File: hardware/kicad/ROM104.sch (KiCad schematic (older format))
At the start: 27 parts, among them J1 Screw_Terminal_01x12, J2 CAN, K1 DIPxx-1Cxx-51x, K2 DIPxx-1Cxx-51x, K3 DIPxx-1Cxx-51x, K4 DIPxx-1Cxx-51x, SW1 INSTANCE, SW2 BUS, U1 L293D, U2 L293D, U3 MCP2551-I-P, U4 TMR_2411, U5 Teensy_3.2

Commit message: Update PCB
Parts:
- removed K1, K2, K3, K4: DIPxx-1Cxx-51x, PDJR-connectors:PE014F05, symbol Relay:DIPxx-1Cxx-51x
- removed R1, R2, R3, R4: 470R, Resistor_THT:R_Axial_DIN0207_L6.3mm_D2.5mm_P7.62mm_Horizontal, symbol Device:R
- added K1, K2, K3, K4: SPDT_RELAY, PDJR-connectors:PE014F05, symbol pdjr:SPDT_RELAY
- added RN1: 470R, Resistor_THT:R_Array_SIP5, symbol Device:R_Network04
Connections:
- net CH0_LED: now also D1.2 (A), U5.2 (D0/RX1); no longer U5.3 (D1/TX1)
- net CH1_LED: now also D2.2 (A), U5.3 (D1/TX1); no longer U5.2 (D0/RX1)
- net CH2_LED: now also D3.2 (A)
- net CH3_LED: now also D4.2 (A)
- net GND: now also RN1.1 (common); no longer D1.1 (K), D2.1 (K), D3.1 (K), D4.1 (K)
- net at J1.1 (Pin_1): now also K1.14
- net at J1.10 (Pin_10): now also K4.14
- net at J1.11 (Pin_11): now also K4.7
- net at J1.12 (Pin_12): now also K4.1
- net at J1.2 (Pin_2): now also K1.7
- net at J1.3 (Pin_3): now also K1.1
- net at J1.4 (Pin_4): now also K2.14
- net at J1.5 (Pin_5): now also K2.7
- net at J1.6 (Pin_6): now also K2.1
- net at J1.7 (Pin_7): now also K3.14
- net at J1.8 (Pin_8): now also K3.7
- net at J1.9 (Pin_9): now also K3.1
- net at U2.11 (3Y): now also K1.6
- net at U2.14 (4Y): now also K1.2
- net at U2.3 (1Y): now also K2.6
- net at U2.6 (2Y): now also K2.2
- net at U1.11 (3Y): now also K3.6
- net at U1.14 (4Y): now also K3.2
- net at U1.3 (1Y): now also K4.6
- net at U1.6 (2Y): now also K4.2
- new net: D1.1 (K), RN1.5 (R4)
- new net: D2.1 (K), RN1.4 (R3)
- new net: D3.1 (K), RN1.3 (R2)
- new net: D4.1 (K), RN1.2 (R1)
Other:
- moved on the sheet: D1, D2, D3, D4
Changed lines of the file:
@@
 Wire Wire Line
 	10450 1150 10450 2150
+Text Label 9550 5350 0    50   ~ 0
+CH0_LED
 Text Label 9550 5250 0    50   ~ 0
-CH0_LED
-Text Label 9550 5350 0    50   ~ 0
 CH1_LED
 Text Label 9550 5150 0    50   ~ 0
@@
 CH3_LED
 $Comp
-L Device:R R1
-U 1 1 631C1A0C
+L Device:LED D1
+U 1 1 631C329D
 P 4400 800
-F 0 "R1" V 4450 1000 50  0000 R CNN
-F 1 "470R" V 4400 800 39  0000 C CNN
-F 2 "Resistor_THT:R_Axial_DIN0207_L6.3mm_D2.5mm_P7.62mm_Horizontal" V 4330 800 50  0001 C CNN
+F 0 "D1" H 4500 750 50  0000 C CNN
+F 1 "LED" H 4393 636 50  0001 C CNN
+F 2 "LED_THT:LED_D1.8mm_W3.3mm_H2.4mm" H 4400 800 50  0001 C CNN
 F 3 "~" H 4400 800 50  0001 C CNN
 	1    4400 800
-	0    -1   -1   0
-$EndComp
-$Comp
-L Device:LED D1
-U 1 1 631C329D
-P 4800 800
-F 0 "D1" H 4900 750 50  0000 C CNN
-F 1 "LED" H 4793 636 50  0001 C CNN
-F 2 "LED_THT:LED_D1.8mm_W3.3mm_H2.4mm" H 4800 800 50  0001 C CNN
-F 3 "~" H 4800 800 50  0001 C CNN
-	1    4800 800
-	-1   0    0    1
-$EndComp
-Wire Wire Line
-	4550 800  4650 800
+	-1   0    0    1
+$EndComp
 Wire Wire Line
 	4050 800  4250 800
-Wire Wire Line
-	4950 800  5450 800
-Wire Wire Line
-	5450 800  5450 1000
-$Comp
-L Device:R R2
-U 1 1 631D6F98
+$Comp
+L Device:LED D2
+U 1 1 631D7AEF
 P 4400 1000
-F 0 "R2" V 4450 1250 50  0000 R CNN
-F 1 "470R" V 4400 1000 39  0000 C CNN
-F 2 "Resistor_THT:R_Axial_DIN0207_L6.3mm_D2.5mm_P7.62mm_Horizontal" V 4330 1000 50  0001 C CNN
+F 0 "D2" H 4500 950 50  0000 C CNN
+F 1 "LED" H 4393 836 50  0001 C CNN
+F 2 "LED_THT:LED_D1.8mm_W3.3mm_H2.4mm" H 4400 1000 50  0001 C CNN
 F 3 "~" H 4400 1000 50  0001 C CNN
 	1    4400 1000
-	0    -1   -1   0
-$EndComp
-$Comp
-L Device:R R3
-U 1 1 631D739B
+	-1   0    0    1
+$EndComp
+$Comp
+L Device:LED D3
+U 1 1 631D7EE7
 P 4400 1200
-F 0 "R3" V 4450 1450 50  0000 R CNN
-F 1 "470R" V 4400 1200 39  0000 C CNN
-F 2 "Resistor_THT:R_Axial_DIN0207_L6.3mm_D2.5mm_P7.62mm_Horizontal" V 4330 1200 50  0001 C CNN
+F 0 "D3" H 4500 1150 50  0000 C CNN
+F 1 "LED" H 4393 1036 50  0001 C CNN
+F 2 "LED_THT:LED_D1.8mm_W3.3mm_H2.4mm" H 4400 1200 50  0001 C CNN
 F 3 "~" H 4400 1200 50  0001 C CNN
 	1    4400 1200
-	0    -1   -1   0
-$EndComp
-$Comp
-L Device:R R4
-U 1 1 631D7696
+	-1   0    0    1
+$EndComp
+$Comp
+L Device:LED D4
+U 1 1 631D8355
 P 4400 1400
-F 0 "R4" V 4450 1650 50  0000 R CNN
-F 1 "470R" V 4400 1400 39  0000 C CNN
-F 2 "Resistor_THT:R_Axial_DIN0207_L6.3mm_D2.5mm_P7.62mm_Horizontal" V 4330 1400 50  0001 C CNN
+F 0 "D4" H 4500 1350 50  0000 C CNN
+F 1 "LED" H 4393 1236 50  0001 C CNN
+F 2 "LED_THT:LED_D1.8mm_W3.3mm_H2.4mm" H 4400 1400 50  0001 C CNN
 F 3 "~" H 4400 1400 50  0001 C CNN
 	1    4400 1400
-	0    -1   -1   0
-$EndComp
-$Comp
-L Device:LED D2
-U 1 1 631D7AEF
-P 4800 1000
-F 0 "D2" H 4900 950 50  0000 C CNN
-F 1 "LED" H 4793 836 50  0001 C CNN
-F 2 "LED_THT:LED_D1.8mm_W3.3mm_H2.4mm" H 4800 1000 50  0001 C CNN
-F 3 "~" H 4800 1000 50  0001 C CNN
-	1    4800 1000
-	-1   0    0    1
-$EndComp
-$Comp
-L Device:LED D3
-U 1 1 631D7EE7
-P 4800 1200
-F 0 "D3" H 4900 1150 50  0000 C CNN
-F 1 "LED" H 4793 1036 50  0001 C CNN
-F 2 "LED_THT:LED_D1.8mm_W3.3mm_H2.4mm" H 4800 1200 50  0001 C CNN
-F 3 "~" H 4800 1200 50  0001 C CNN
-	1    4800 1200
-	-1   0    0    1
-$EndComp
-$Comp
-L Device:LED D4
-U 1 1 631D8355
-P 4800 1400
-F 0 "D4" H 4900 1350 50  0000 C CNN
-F 1 "LED" H 4793 1236 50  0001 C CNN
-F 2 "LED_THT:LED_D1.8mm_W3.3mm_H2.4mm" H 4800 1400 50  0001 C CNN
-F 3 "~" H 4800 1400 50  0001 C CNN
-	1    4800 1400
 	-1   0    0    1
 $EndComp
@@
 Wire Wire Line
 	4550 1200 4650 1200
-Wire Wire Line
-	4550 1400 4650 1400
-Wire Wire Line
-	4950 1000 5450 1000
-Connection ~ 5450 1000
-Wire Wire Line
-	5450 1000 5450 1200
-Wire Wire Line
-	4950 1200 5450 1200
-Connection ~ 5450 1200
-Wire Wire Line
-	5450 1200 5450 1400
-Wire Wire Line
-	4950 1400 5450 1400
-Connection ~ 5450 1400
-Wire Wire Line
-	5450 1400 5450 1500
 $Comp
 L power:GND #PWR04
 U 1 1 632040BF
-P 5450 1500
-F 0 "#PWR04" H 5450 1250 50  0001 C CNN
-F 1 "GND" H 5455 1327 50  0000 C CNN
-F 2 "" H 5450 1500 50  0001 C CNN
-F 3 "" H 5450 1500 50  0001 C CNN
-	1    5450 1500
+P 5250 1350
+F 0 "#PWR04" H 5250 1100 50  0001 C CNN
+F 1 "GND" H 5255 1177 50  0000 C CNN
+F 2 "" H 5250 1350 50  0001 C CNN
+F 3 "" H 5250 1350 50  0001 C CNN
+	1    5250 1350
 	1    0    0    -1
 $EndComp
@@
 	-1   0    0    1
 $EndComp
-$Comp
-L Relay:DIPxx-1Cxx-51x K2
-U 1 1 632F5385
-P 2250 4400
-F 0 "K2" H 1820 4354 50  0000 R CNN
-F 1 "DIPxx-1Cxx-51x" H 1820 4445 50  0000 R CNN
-F 2 "PDJR-connectors:PE014F05" H 2700 4350 50  0001 L CNN
-F 3 "https://standexelectronics.com/wp-content/uploads/datasheet_reed_relay_DIP.pdf" H 2250 4400 50  0001 C CNN
-	1    2250 4400
-	-1   0    0    1
-$EndComp
 Wire Wire Line
 	2150 4700 2150 5100
@@
 Wire Wire Line
 	2050 4000 2050 4100
-$Comp
-L Relay:DIPxx-1Cxx-51x K3
-U 1 1 63338136
-P 2250 5600
-F 0 "K3" H 1820 5554 50  0000 R CNN
-F 1 "DIPxx-1Cxx-51x" H 1820 5645 50  0000 R CNN
-F 2 "PDJR-connectors:PE014F05" H 2700 5550 50  0001 L CNN
-F 3 "https://standexelectronics.com/wp-content/uploads/datasheet_reed_relay_DIP.pdf" H 2250 5600 50  0001 C CNN
-	1    2250 5600
-	-1   0    0    1
-$EndComp
 Wire Wire Line
 	1950 5900 1950 6000
@@
 Wire Wire Line
 	1650 5400 1650 6100
-$Comp
-L Relay:DIPxx-1Cxx-51x K1
-U 1 1 63388BFA
-P 2250 3400
-F 0 "K1" H 1820 3354 50  0000 R CNN
-F 1 "DIPxx-1Cxx-51x" H 1820 3445 50  0000 R CNN
-F 2 "PDJR-connectors:PE014F05" H 2700 3350 50  0001 L CNN
-F 3 "https://standexelectronics.com/wp-content/uploads/datasheet_reed_relay_DIP.pdf" H 2250 3400 50  0001 C CNN
-	1    2250 3400
-	-1   0    0    1
-$EndComp
 Wire Wire Line
 	1600 3900 2150 3900
@@
 Wire Wire Line
 	2050 3000 1400 3000
-$Comp
-L Relay:DIPxx-1Cxx-51x K4
-U 1 1 633A9E65
-P 2250 6600
-F 0 "K4" H 1820 6554 50  0000 R CNN
-F 1 "DIPxx-1Cxx-51x" H 1820 6645 50  0000 R CNN
-F 2 "PDJR-connectors:PE014F05" H 2700 6550 50  0001 L CNN
-F 3 "https://standexelectronics.com/wp-content/uploads/datasheet_reed_relay_DIP.pdf" H 2250 6600 50  0001 C CNN
-	1    2250 6600
-	-1   0    0    1
-$EndComp
 Wire Wire Line
 	1200 5500 1450 5500
@@
 	-1   0    0    -1
 $EndComp
+$Comp
+L pdjr:SPDT_RELAY K1
+U 1 1 632C2C12
+P 2250 3400
+F 0 "K1" H 1820 3354 50  0000 R CNN
+F 1 "SPDT_RELAY" H 1820 3445 50  0000 R CNN
+F 2 "PDJR-connectors:PE014F05" H 2700 3350 50  0001 L CNN
+F 3 "https://standexelectronics.com/wp-content/uploads/datasheet_reed_relay_DIP.pdf" H 2250 3400 50  0001 C CNN
+	1    2250 3400
+	-1   0    0    1
+$EndComp
+$Comp
+L pdjr:SPDT_RELAY K2
+U 1 1 632D0338
+P 2250 4400
+F 0 "K2" H 1820 4354 50  0000 R CNN
+F 1 "SPDT_RELAY" H 1820 4445 50  0000 R CNN
+F 2 "PDJR-connectors:PE014F05" H 2700 4350 50  0001 L CNN
+F 3 "https://standexelectronics.com/wp-content/uploads/datasheet_reed_relay_DIP.pdf" H 2250 4400 50  0001 C CNN
+	1    2250 4400
+	-1   0    0    1
+$EndComp
+$Comp
+L pdjr:SPDT_RELAY K3
+U 1 1 632D258A
+P 2250 5600
+F 0 "K3" H 1820 5554 50  0000 R CNN
+F 1 "SPDT_RELAY" H 1820 5645 50  0000 R CNN
+F 2 "PDJR-connectors:PE014F05" H 2700 5550 50  0001 L CNN
+F 3 "https://standexelectronics.com/wp-content/uploads/datasheet_reed_relay_DIP.pdf" H 2250 5600 50  0001 C CNN
+	1    2250 5600
+	-1   0    0    1
+$EndComp
+$Comp
+L pdjr:SPDT_RELAY K4
+U 1 1 632D3E33
+P 2250 6600
+F 0 "K4" H 1820 6554 50  0000 R CNN
+F 1 "SPDT_RELAY" H 1820 6645 50  0000 R CNN
+F 2 "PDJR-connectors:PE014F05" H 2700 6550 50  0001 L CNN
+F 3 "https://standexelectronics.com/wp-content/uploads/datasheet_reed_relay_DIP.pdf" H 2250 6600 50  0001 C CNN
+	1    2250 6600
+	-1   0    0    1
+$EndComp
+$Comp
+L Device:R_Network04 RN1
+U 1 1 632DFEEA
+P 5050 1050
+F 0 "RN1" V 5375 1050 50  0000 C CNN
+F 1 "470R" V 5284 1050 50  0000 C CNN
+F 2 "Resistor_THT:R_Array_SIP5" V 5325 1050 50  0001 C CNN
+F 3 "http://www.vishay.com/docs/31509/csc.pdf" H 5050 1050 50  0001 C CNN
+	1    5050 1050
+	0    1    -1   0
+$EndComp
+Wire Wire Line
+	4750 800  4750 950
+Wire Wire Line
+	4750 950  4850 950
+Wire Wire Line
+	4550 800  4750 800
+Wire Wire Line
+	4750 1400 4750 1250
+Wire Wire Line
+	4750 1250 4850 1250
+Wire Wire Line
+	4550 1400 4750 1400
+Wire Wire Line
+	4650 1200 4650 1150
+Wire Wire Line
+	4650 1150 4850 1150
+Wire Wire Line
+	4650 1000 4650 1050
+Wire Wire Line
+	4650 1050 4850 1050
+Wire Wire Line
+	5250 1250 5250 1350
 $EndSCHEMATC

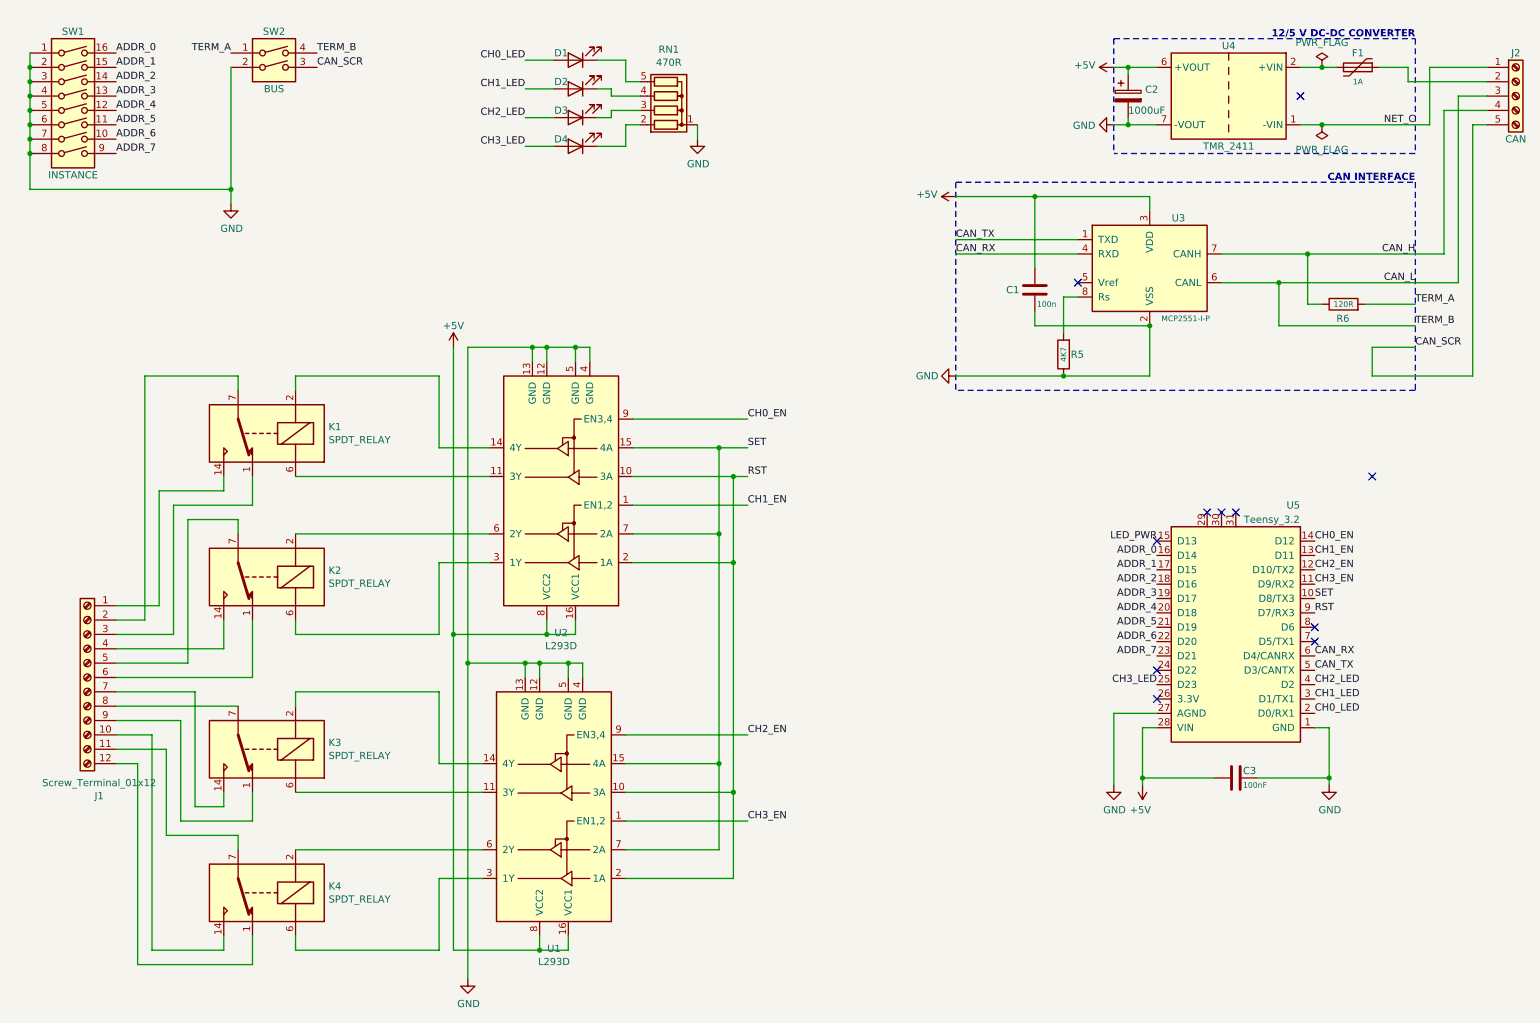
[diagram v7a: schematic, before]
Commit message: PCB resize
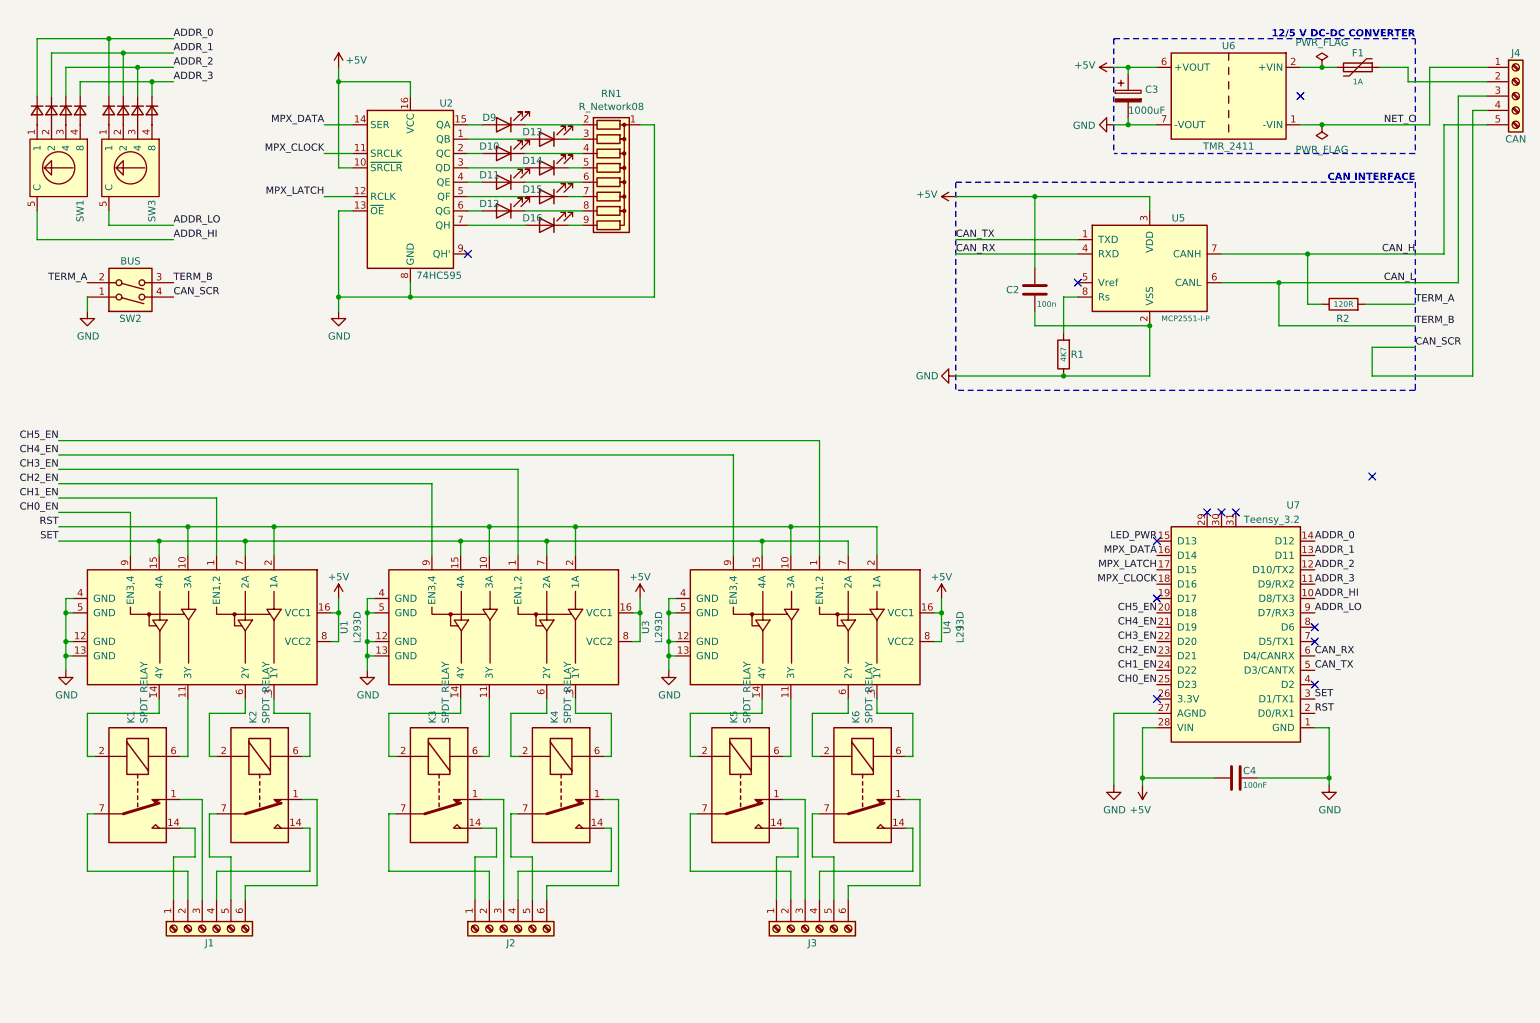
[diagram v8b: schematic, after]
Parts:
- removed J1: Screw_Terminal_01x12, PDJR-connectors:WURTH-401B-12PIN, symbol Connector:Screw_Terminal_01x12
- removed RN1: 470R, Resistor_THT:R_Array_SIP5, symbol Device:R_Network04
- removed SW1: INSTANCE, Package_DIP:DIP-16_W7.62mm, symbol Switch:SW_DIP_x08
- removed U1: L293D, Package_DIP:DIP-16_W7.62mm, symbol Driver_Motor:L293D
- added D1, D2, D3, D4, D5, D6, D7, D8: D_Small, Diode_THT:D_DO-34_SOD68_P2.54mm_Vertical_AnodeUp, symbol Device:D_Small
- added D11, D12, D15, D16: LED, LED_THT:LED_D1.8mm_W3.3mm_H2.4mm, symbol Device:LED
- added J1, J2, J3: Screw_Terminal_01x06, PDJR-connectors:879-1272_TERMINAL_HEADER_6-POLE, symbol Connector:Screw_Terminal_01x06
- added K5, K6: SPDT_RELAY, PDJR-connectors:PE014F05, symbol pdjr:SPDT_RELAY
- added RN1: R_Network08, Resistor_THT:R_Array_SIP9, symbol Device:R_Network08
- added SW1, SW3: HEX_ENCODER, PDJR-connectors:FR01-SR16P-ST, symbol pdjr:HEX_ENCODER
- added U2: 74HC595, Package_DIP:DIP-16_W7.62mm_Socket_LongPads, symbol 74xx:74HC595
- added U3, U4: L293D, Package_DIP:DIP-16_W7.62mm, symbol Driver_Motor:L293D
- renumbered C1 to C2, C2 to C3, C3 to C4, D3 to D10, D2 to D13, D4 to D14, D1 to D9, J2 to J4, R5 to R1, R6 to R2, U2 to U1, U3 to U5, U4 to U6, U5 to U7
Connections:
- net ADDR_6 is gone; now on net CH3_EN: U7.22 (D20)
- net ADDR_7 is gone; now on net CH2_EN: U7.23 (D21)
- net +5V: now also U2.10 (~SRCLR), U2.16 (VCC), U3.16 (VCC1), U3.8 (VCC2), U4.16 (VCC1), U4.8 (VCC2)
- net ADDR_0: now also U7.14 (D12), D1.1 (K), D5.1 (K); no longer U7.16 (D14)
- net ADDR_1: now also U7.13 (D11), D2.1 (K), D6.1 (K); no longer U7.17 (D15)
- net ADDR_2: now also U7.12 (D10/TX2), D3.1 (K), D7.1 (K); no longer U7.18 (D16)
- net ADDR_3: now also U7.11 (D9/RX2), D4.1 (K), D8.1 (K); no longer U7.19 (D17)
- net CAN_H: now also J4.5 (Pin_5); no longer J4.4 (Pin_4)
- net CAN_L: now also SW2.3; no longer SW2.4
- net CAN_SCR: now also J4.4 (Pin_4), SW2.4; no longer J4.5 (Pin_5), SW2.3
- net CH0_EN: now also U7.25 (D23); no longer U7.14 (D12)
- net CH1_EN: now also U7.24 (D22); no longer U7.13 (D11)
- net CH2_EN: now also U3.9 (EN3,4); no longer U7.12 (D10/TX2)
- net CH3_EN: now also U3.1 (EN1,2); no longer U7.11 (D9/RX2)
- net GND: now also SW2.1, RN1.1 (common), U2.13 (~OE), U2.8 (GND), U3.12 (GND), U3.13 (GND), U3.4 (GND), U3.5 (GND), U4.12 (GND), U4.13 (GND), U4.4 (GND), U4.5 (GND); no longer SW2.2
- net RST: now also U7.2 (D0/RX1), U3.10 (3A), U3.2 (1A), U4.10 (3A), U4.2 (1A); no longer U7.9 (D7/RX3)
- net SET: now also U7.3 (D1/TX1), U3.15 (4A), U3.7 (2A), U4.15 (4A), U4.7 (2A); no longer U7.10 (D8/TX3)
- net TERM_A: now also SW2.2; no longer SW2.1
- net at D9.1 (K): now also RN1.2 (R1)
- net at K1.14: now also J1.1 (Pin_1)
- net at K4.14: now also J2.4 (Pin_4)
- net at K4.7: now also J2.5 (Pin_5)
- net at K4.1: now also J2.6 (Pin_6)
- net at K1.7: now also J1.2 (Pin_2)
- net at K1.1: now also J1.3 (Pin_3)
- net at K2.14: now also J1.4 (Pin_4)
- net at K2.7: now also J1.5 (Pin_5)
- net at K2.1: now also J1.6 (Pin_6)
- net at K3.14: now also J2.1 (Pin_1)
- net at K3.7: now also J2.2 (Pin_2)
- net at K3.1: now also J2.3 (Pin_3)
- net at D13.1 (K): now also RN1.3 (R2)
- net at D10.1 (K): now also RN1.4 (R3)
- net at D14.1 (K): now also RN1.5 (R4)
- net at K3.6: now also U3.11 (3Y)
- net at K3.2: now also U3.14 (4Y)
- net at K4.6: now also U3.3 (1Y)
- net at K4.2: now also U3.6 (2Y)
- net ADDR_4 renamed CH5_EN
- net CH5_EN: now also U4.1 (EN1,2)
- net ADDR_5 renamed CH4_EN
- net CH4_EN: now also U4.9 (EN3,4)
- net CH0_LED: no longer names the net of D9.2 (A)
- net CH0_LED: now also U2.15 (QA); no longer U7.2 (D0/RX1)
- net CH1_LED: no longer names the net of D13.2 (A)
- net CH1_LED: now also U2.1 (QB); no longer U7.3 (D1/TX1)
- net CH2_LED: no longer names the net of U7.4 (D2)
- net CH2_LED: no longer D10.2 (A)
- net CH3_LED: no longer names the net of D14.2 (A)
- net CH3_LED: now also U2.3 (QD); no longer U7.25 (D23)
- new net: D10.2 (A), U2.2 (QC)
- new net: D12.1 (K), RN1.8 (R7)
- new net: D12.2 (A), U2.6 (QG)
- new net: D16.1 (K), RN1.9 (R8)
- new net: D16.2 (A), U2.7 (QH)
- new net: D11.1 (K), RN1.6 (R5)
- new net: D15.1 (K), RN1.7 (R6)
- new net: D11.2 (A), U2.4 (QE)
- new net: D15.2 (A), U2.5 (QF)
- new net: K5.6, U4.11 (3Y)
- new net: K5.2, U4.14 (4Y)
- new net: K6.6, U4.3 (1Y)
- new net: K6.2, U4.6 (2Y)
- new net: J3.3 (Pin_3), K5.1
- new net: J3.1 (Pin_1), K5.14
- new net: J3.2 (Pin_2), K5.7
- new net: J3.4 (Pin_4), K6.14
- new net: J3.5 (Pin_5), K6.7
- new net: J3.6 (Pin_6), K6.1
- new net: D1.2 (A), SW1.1
- new net: D2.2 (A), SW1.2
- new net: D3.2 (A), SW1.3 (4)
- new net: D4.2 (A), SW1.4 (8)
- new net: D5.2 (A), SW3.1
- new net: D6.2 (A), SW3.2
- new net: D7.2 (A), SW3.3 (4)
- new net: D8.2 (A), SW3.4 (8)
- new net ADDR_HI: SW1.5 (C), U7.10 (D8/TX3)
- new net ADDR_LO: SW3.5 (C), U7.9 (D7/RX3)
- new net MPX_CLOCK: U2.11 (SRCLK), U7.18 (D16)
- new net MPX_DATA: U2.14 (SER), U7.16 (D14)
- new net MPX_LATCH: U2.12 (RCLK), U7.17 (D15)
- no-connect marks 11 -> 13
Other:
- moved on the sheet: D10, D13, D14, D9, K1, K2, SW2, U1
